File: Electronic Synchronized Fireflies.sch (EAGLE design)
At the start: 42 parts, among them Q1 NPN, Q2 DMP2035U-7, U2 MSP430G2231/TSSOP-14, X1 22-23-2021, X2 22-23-2031, X3 22-23-2021

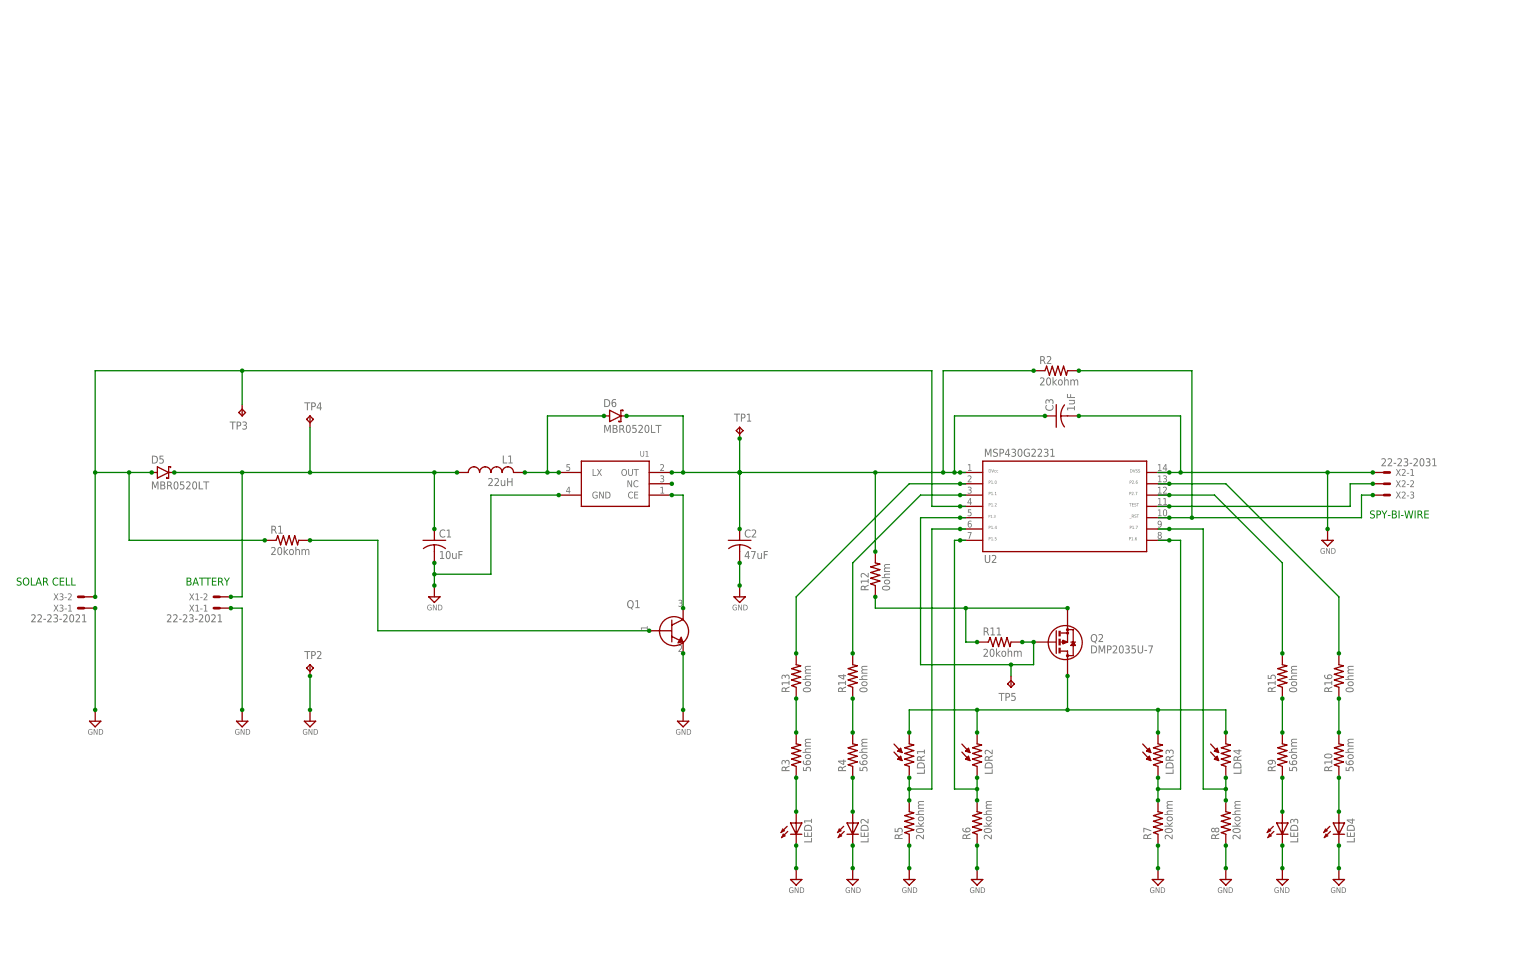
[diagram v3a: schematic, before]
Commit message: Reduced number of parts, LDRs to phototransistors
v1.1 Changed from 4 pairs of LEDs and LDRs to three pairs of LEDs and
phototransistors. Replaced power transistor with MOSFET and solar cell
connection with surface mount photocell.
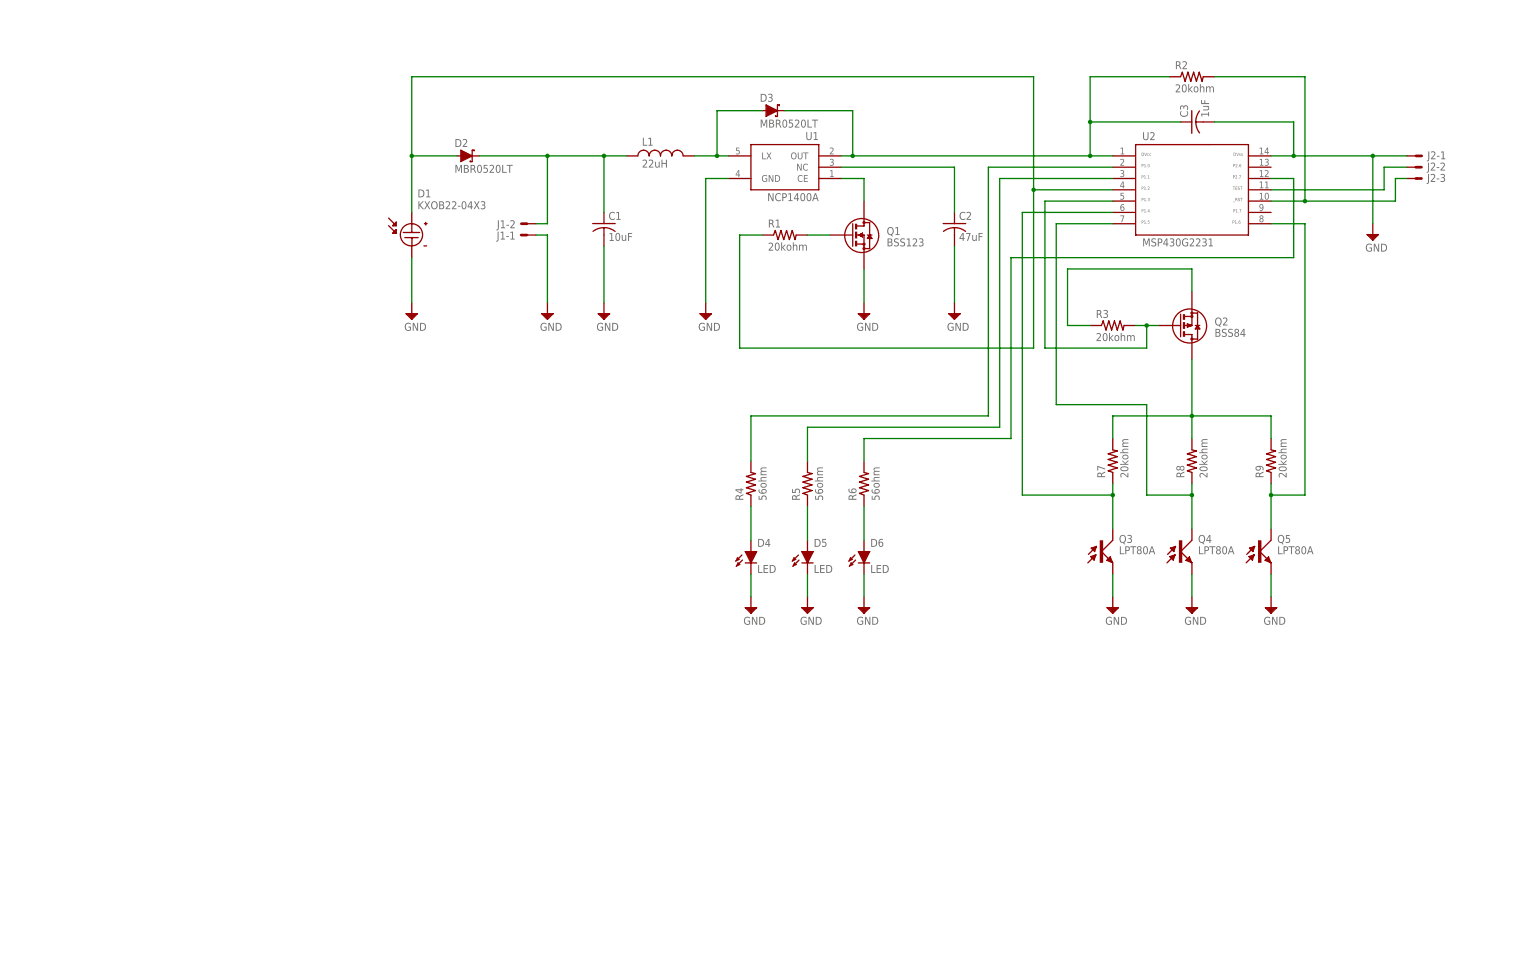
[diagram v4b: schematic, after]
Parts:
- removed LDR1, LDR2, LDR3, LDR4: LDR, Firefly:LDR
- removed LED1, LED2, LED3, LED4: (no value), Firefly:LED5MM
- removed R10: 56ohm, Firefly:RESISTORSR0805
- removed R11: 20kohm, Firefly:RESISTORSR0805
- removed R12, R13, R14, R15, R16: 0ohm, Firefly:RESISTORSR0805
- removed TP1, TP2, TP3, TP4, TP5: TPTP08SQ, Firefly:TPTP08SQ
- removed X1, X3: 22-23-2021, Firefly:22-23-2021
- removed X2: 22-23-2031, Firefly:22-23-2031
- added D1: KXOB22-04X3, Electronic Synchronized Fireflies:KXOB22-04X3
- added D2, D3: MBR0520LT, Electronic Synchronized Fireflies:MBR0520LT
- added D4: LED, Electronic Synchronized Fireflies:LED
- added J1: 2WIRE_HEADER, Electronic Synchronized Fireflies:2WIRE_HEADER
- added J2: 3WIRE_HEADER, Electronic Synchronized Fireflies:3WIRE_HEADER
- added Q3, Q4, Q5: LPT80A, Electronic Synchronized Fireflies:LPT80A
- C1, C2, C3: device Firefly:CAPACITORC0805 -> Electronic Synchronized Fireflies:CAPACITOR
- D5, D6: value MBR0520LT -> LED; device Firefly:MBR0520LT -> Electronic Synchronized Fireflies:LED
- L1: device Firefly:L-US -> Electronic Synchronized Fireflies:INDUCTOR
- Q1: value NPN -> BSS123; device Firefly:NPN -> Electronic Synchronized Fireflies:BSS123
- Q2: value DMP2035U-7 -> BSS84; device Firefly:BSS84 -> Electronic Synchronized Fireflies:BSS84
- R1, R2, R4, R7, R8: device Firefly:RESISTORSR0805 -> Electronic Synchronized Fireflies:RESISTOR
- R3, R9: value 56ohm -> 20kohm; device Firefly:RESISTORSR0805 -> Electronic Synchronized Fireflies:RESISTOR
- R5, R6: value 20kohm -> 56ohm; device Firefly:RESISTORSR0805 -> Electronic Synchronized Fireflies:RESISTOR
- U1: value (none) -> NCP1400A; device Firefly:NCP1400A -> Electronic Synchronized Fireflies:NCP1400A
- U2: value MSP430G2231/TSSOP-14 -> MSP430G2231; device Firefly:MSP430G2231/TSSOP-14 -> Electronic Synchronized Fireflies:MSP430G2231
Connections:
- removed net N$19: R13.1, R3.2
- removed net N$23: R15.2, U2.12
- removed net N$24: LED1.A, R3.1
- removed net N$25: R10.2, R16.1
- removed net N$26: R15.1, R9.2
- removed net N$29: LDR3.1, R7.2, U2.8
- removed net N$30: LDR4.1, R8.2, U2.9
- removed net N$31: LED3.A, R9.1
- removed net N$32: LED4.A, R10.1
- new net N$6: Q1.S, U1.CE
- new net N$9: J2-3.S, R2.P$2, U2.10
- net GND: now also D1.-, D4.C, D5.C, D6.C, J1-1.S, J2-1.S, Q1.D, Q3.E, Q4.E, Q5.E; no longer LED1.C, LED2.C, LED3.C, LED4.C, Q1.E, R5.1, R6.1, R7.1, R8.1, TP2.TP, X1-1.S, X2-1.S, X3-1.S
- net N$1: now also C1.1, D2.C, J1-2.S, L1.1; no longer LDR1.2, LDR2.2, LDR3.2, LDR4.2, Q2.D
- net N$10: now also Q2.S, R3.P$1; no longer Q1.C, U1.CE
- net N$11: now also J2-2.S, U2.11; no longer R13.2, U2.2
- net N$12: now also Q2.D, R7.P$2, R8.P$2, R9.P$2; no longer R14.2, U2.3
- net N$13: now also Q4.C, R8.P$1, U2.7; no longer D5.A, R1.1, TP3.TP, U2.4, X3-2.S
- net N$14: now also Q3.C, R7.P$1, U2.6; no longer R2.2, U2.10, X2-3.S
- net N$15: now also Q5.C, R9.P$1, U2.8; no longer Q2.S, R11.1, R12.1
- net N$16: now also R4.P$2, U2.2; no longer LDR2.1, R6.2, U2.7
- net N$17: now also R5.P$2, U2.3; no longer LDR1.1, R5.2, U2.6
- net N$18: now also R6.P$2, U2.12; no longer LED2.A, R4.1
- net N$2: now also D1.+, D2.A, R1.P$1, U2.4; no longer Q1.B, R1.2
- net N$20: now also D5.A, R5.P$1; no longer U2.11, X2-2.S
- net N$21: now also D6.A, R6.P$1; no longer R16.2, U2.13
- net N$22: now also D4.A, R4.P$1; no longer R14.1, R4.2
- net N$3: now also D3.A, L1.2, U1.LX; no longer Q2.G, R11.2, TP5.TP, U2.5
- net N$4: now also Q2.G, R3.P$2, U2.5; no longer C1.1, D5.C, L1.1, TP4.TP, X1-2.S
- net N$5: now also C3.1, D3.C, R2.P$1, U1.OUT, U2.1; no longer D6.A, L1.2, U1.LX
- net N$7: now also Q1.G, R1.P$2; no longer U1.NC
- net N$8: now also U1.NC; no longer C3.1, D6.C, R12.2, R2.1, TP1.TP, U1.OUT, U2.1
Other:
- note removed: "BATTERY"
- note removed: "SOLAR CELL"
- note removed: "SPY-BI-WIRE"
- moved on the sheet: C1, C2, C3, L1, Q2, R1, R2, R3, R4, R5, R6, R7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

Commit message: Updated board / schematic / library
Smaller PCB footprint, added frames to board layout.
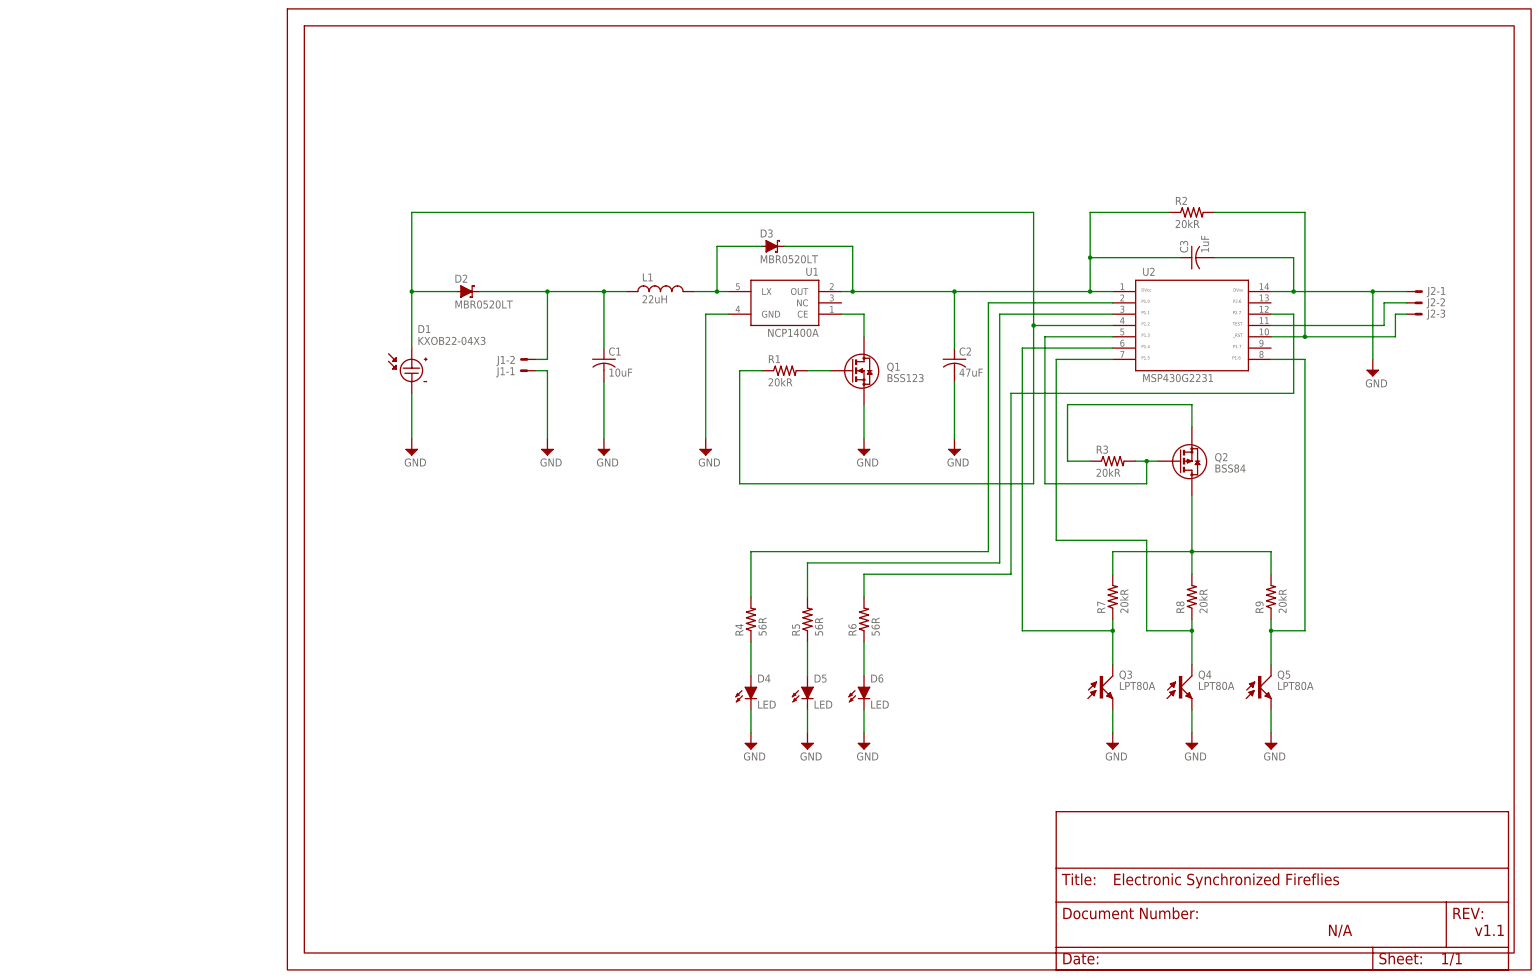
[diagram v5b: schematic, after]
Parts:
- added FRAME1: (no value), Electronic Synchronized Fireflies:FRAME_A_L
- added U$1: DOCFIELD, Electronic Synchronized Fireflies:DOCFIELD
- D4, D5, D6: device Electronic Synchronized Fireflies:LED -> Electronic Synchronized Fireflies:LEDRTANGLEHOLDER
- Q3, Q4, Q5: device Electronic Synchronized Fireflies:LPT80A -> Electronic Synchronized Fireflies:LPT80ARTANGLEHOLDER
- R1, R2, R3, R7, R8, R9: value 20kohm -> 20kR
- R4, R5, R6: value 56ohm -> 56R
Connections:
- removed net N$8: C2.1, U1.NC
- net N$5: now also C2.1
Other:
- note added: "N/A"
- note added: "v1.1"
- moved on the sheet: C1, C2, C3, D1, D2, D3, D4, D5, D6, J1-1, J1-2, J2-1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

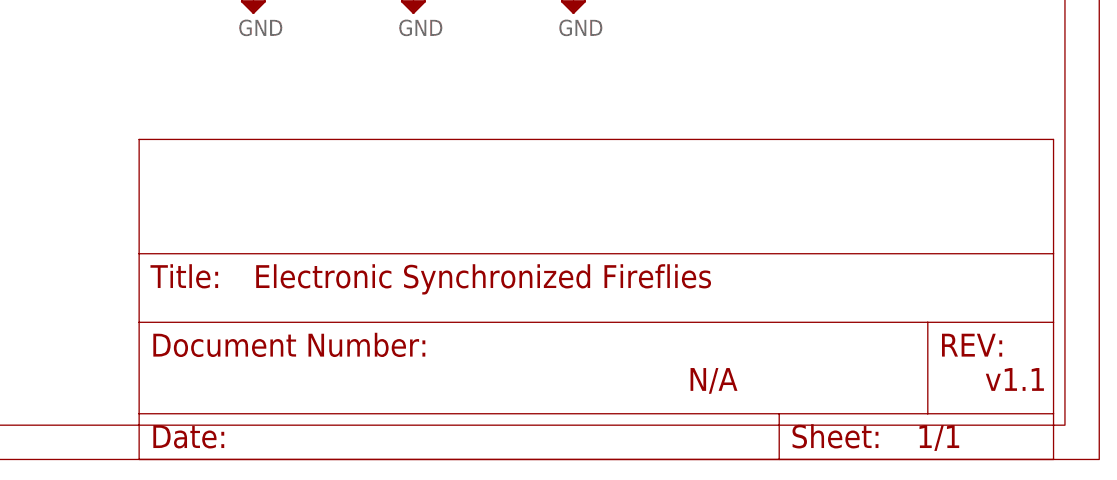
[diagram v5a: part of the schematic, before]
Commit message: Added detail to document fields (Schematic/PCB)
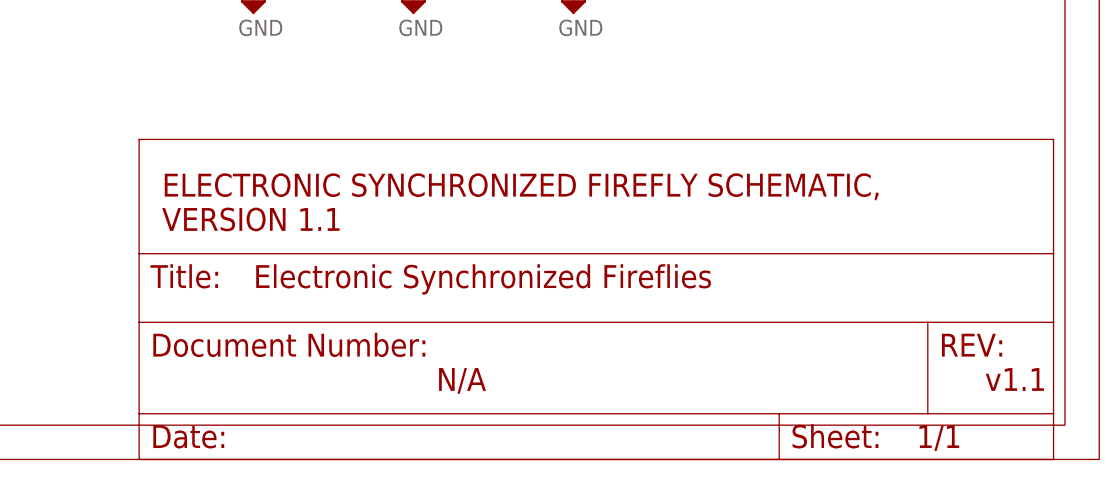
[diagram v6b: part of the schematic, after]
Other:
- note added: "ELECTRONIC SYNCHRONIZED FIREFLY SCHEMATIC, VERSION 1.1"
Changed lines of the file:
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@@
 <setting verticaltext="up"/>
 </settings>
-<grid distance="0.1" unitdist="inch" unit="inch" style="lines" multiple="1" display="no" altdistance="0.01" altunitdist="inch" altunit="inch"/>
+<grid distance="0.1" unitdist="inch" unit="inch" style="lines" multiple="1" display="yes" altdistance="0.01" altunitdist="inch" altunit="inch"/>
 <layers>
 <layer number="1" name="Top" color="4" fill="1" visible="no" active="no"/>
@@
 <plain>
 <text x="266.7" y="7.62" size="2.54" layer="94">v1.1</text>
-<text x="233.68" y="7.62" size="2.54" layer="94">N/A</text>
+<text x="205.74" y="7.62" size="2.54" layer="94">N/A</text>
+<text x="175.26" y="25.4" size="2.54" layer="94">ELECTRONIC SYNCHRONIZED FIREFLY SCHEMATIC,
+VERSION 1.1</text>
 </plain>
 <instances>
@@
 </schematic>
 </drawing>
+<compatibility>
+<note version="6.3" minversion="6.2.2" severity="warning">
+Since Version 6.2.2 text objects can contain more than one line,
+which will not be processed correctly with this version.
+</note>
+</compatibility>
 </eagle>
